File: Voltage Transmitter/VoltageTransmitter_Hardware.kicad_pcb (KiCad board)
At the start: 2 copper layers, 30.5 x 71.9 mm, 8 parts, among them U1 OKI, U2 ESP8266_MCU

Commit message: Gerbs Made
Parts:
- added G***: LOGO, Voltage_Transmitter_Hardware:Austin_Christman_22mmX8.3mm, B.Cu at (127.3, 80.8)
- added G***: LOGO, Voltage_Transmitter_Hardware:John_Beuke_22mmX7.4mm, F.Cu at (138.7, 73.2)
- moved Conn2 2.18 mm to (137.4, 61.7)
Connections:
- C1 pad 2: Net-(C1-Pad2) -> GND
- C2 pad 2: Net-(C1-Pad2) -> GND
- Conn2 pad 1: Net-(C1-Pad2) -> GND
- U1 pad 2: Net-(C1-Pad2) -> GND
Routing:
- net Net-(C1-Pad2): track 26.7 -> 0.00 mm
- net GND: track 5.18 -> 10.3 mm
- net Net-(C1-Pad1): track 18.1 -> 17.1 mm
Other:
- board text added: "Voltage Transmitter, Rev 1 Mars Rover Design Team Missouri S&T, 2019 Austin Christman, John Beuke"
- board text removed: "Voltage Transmitter, Rev 1 Mars Rover Design Team Missouri S&T Austin Christman, John Beuke"

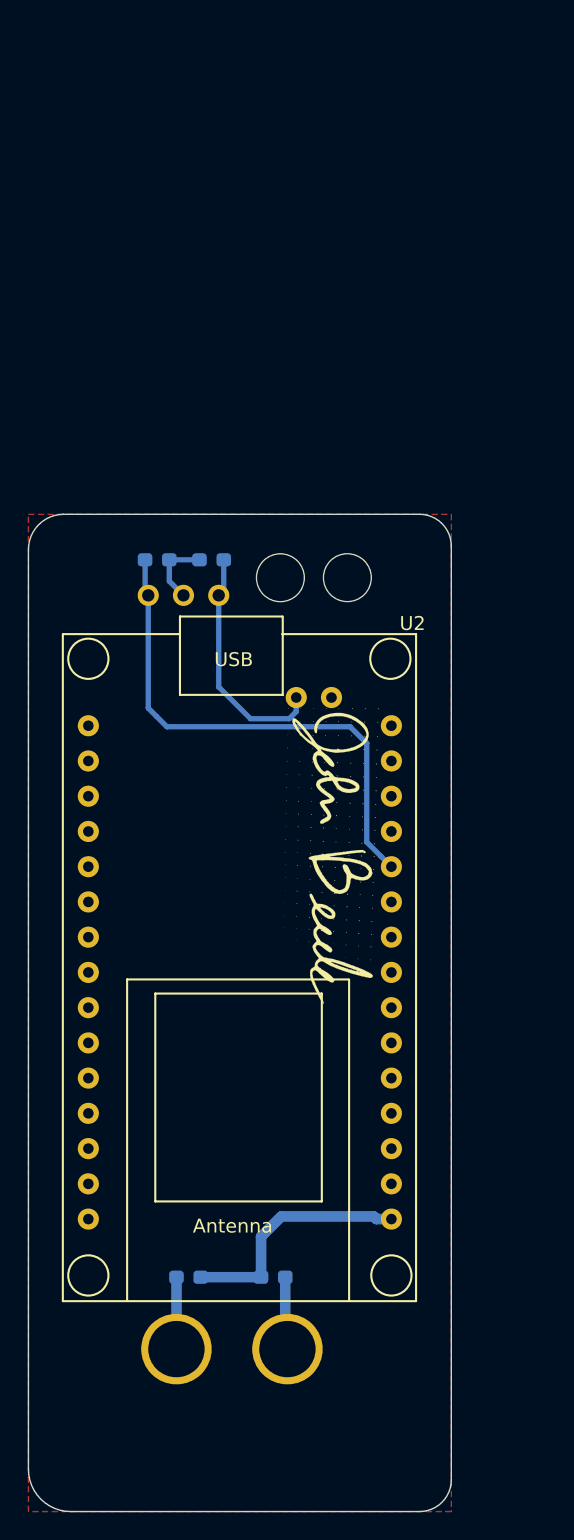
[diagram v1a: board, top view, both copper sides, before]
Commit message: Changed shaped & added comps
Changed to stacked andersons, added power led, transmitting led, and made sure no comps are located on the bottom of the board.
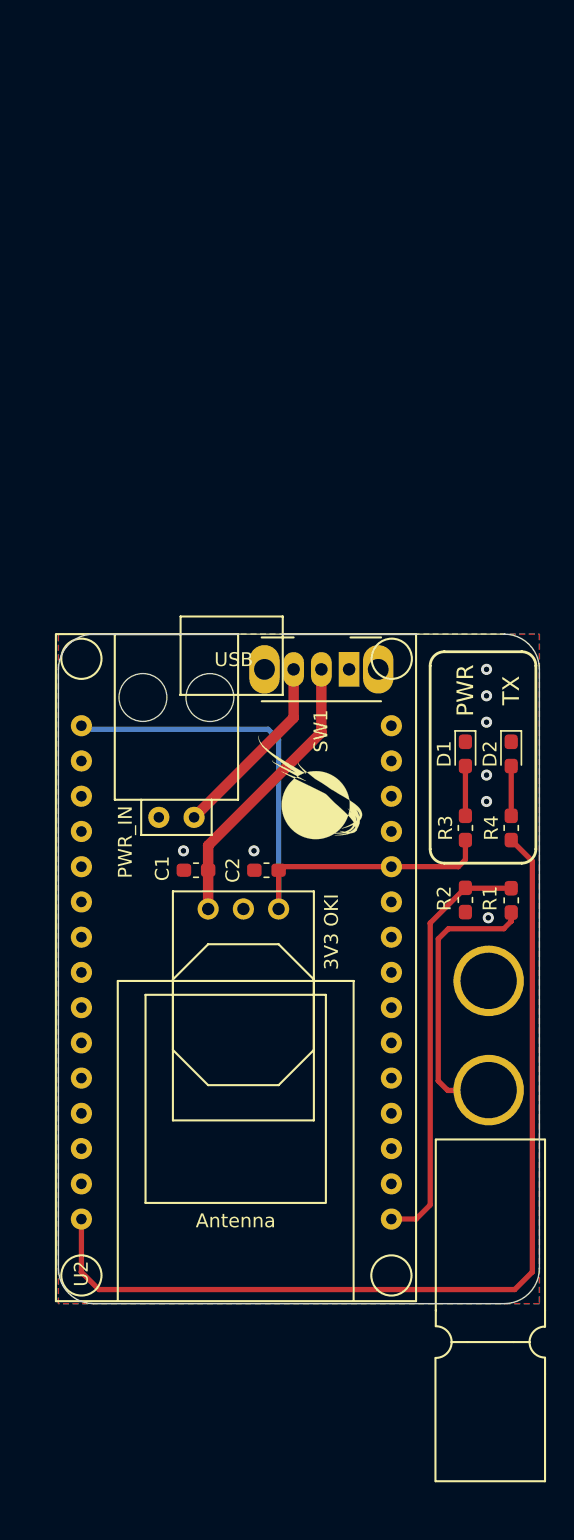
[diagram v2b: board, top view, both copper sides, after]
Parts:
- removed the G*** at (127.3, 80.8)
- added D1: LED, LED_SMD:LED_0603_1608Metric_Pad1.05x0.95mm_HandSolder, F.Cu at (148.3, 65.8)
- added D2: LED, LED_SMD:LED_0603_1608Metric_Pad1.05x0.95mm_HandSolder, F.Cu at (151.6, 65.8)
- added G***: LOGO, MRDT_Silkscreens:z_sig_Jacob_Lipina_Sig_15mm, B.Cu at (128.4, 97.5)
- added G***: LOGO, MRDT_Silkscreens:2_Dahlbot_2.0, B.Cu at (135.8, 68.2)
- added G***: LOGO, MRDT_Silkscreens:0_MRDT_Logo_7.5mm, F.Cu at (137.2, 68.2)
- added R3: 500, Resistor_SMD:R_0603_1608Metric_Pad1.05x0.95mm_HandSolder, F.Cu at (148.3, 71.1)
- added R4: 500, Resistor_SMD:R_0603_1608Metric_Pad1.05x0.95mm_HandSolder, F.Cu at (151.6, 71.1)
- added SW1: SW_Push_SPDT, Button_Switch_THT:SW_CuK_OS102011MA1QN1_SPDT_Angled, F.Cu at (140.0, 59.7)
- C1, C2, Conn2, U1: moved to F.Cu
- Conn1: footprint MRDT_Connectors:Anderson_2_Horisontal_Side_by_Side -> MRDT_Connectors:Anderson_2_Horizontal_Stacked; moved to F.Cu
- G***: moved to B.Cu
- R1: value 100K -> 150K; moved to F.Cu
- R2: value 11K -> 15K; moved to F.Cu
- U2: footprint VoltageTransmitter_Hardware:ESP_8266 NODEMCU -> MRDT_Shields:ESP_8266_NODEMCU
- moved Conn1 34.7 mm to (150.0, 90.0)
- moved R2 33.7 mm to (148.3, 76.3), turned to 270 degrees
- moved R1 32.1 mm to (151.6, 76.3), turned to 90 degrees
- moved C2 23.7 mm to (134.0, 74.2), turned to 180 degrees
- moved U1 23.3 mm to (127.3, 75.7), turned to 0 degrees
- moved C1 22.4 mm to (128.9, 74.2)
- moved G*** 15.7 mm to (125.0, 80.8), turned to 90 degrees
- moved Conn2 13.1 mm to (127.5, 70.4), turned to 0 degrees
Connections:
- Conn1 pad 1: GND -> Net-(Conn1-Pad1)
- Conn1 pad 2: Net-(Conn1-Pad2) -> GND
- Conn2 pad 2: Net-(C1-Pad1) -> Net-(Conn2-Pad2)
- R1 pad 1: Net-(Conn1-Pad2) -> Net-(Conn1-Pad1)
- U2 pad 16: Net-(U2-Pad16) -> +3V3
- U2 pad 30: Net-(U2-Pad30) -> TX_IND
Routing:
- net TX_IND: track 0.00 -> 69.1 mm
- net Net-(Conn1-Pad1): track 0.00 -> 20.6 mm
- net Net-(Conn2-Pad2): track 0.00 -> 13.6 mm
- net Din: track 17.4 -> 30.4 mm
- net GND: track 10.3 -> 2.30 mm, vias 0 -> 8
- net +3V3: track 37.2 -> 44.8 mm
- net Net-(Conn1-Pad2): track 5.25 -> 0.00 mm
- net Net-(D2-Pad2): track 0.00 -> 3.58 mm
- net Net-(D1-Pad2): track 0.00 -> 3.58 mm
- net Net-(C1-Pad1): track 17.1 -> 20.7 mm
- added copper zone on B.Cu, net GND
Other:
- board size 30.5 x 71.9 mm -> 34.7 x 48.3 mm
- board text added: "+"
- board text added: "-"
- board text added: "3V3 OKI"
- board text added: "OFF"
- board text added: "ON"
- board text added: "PWR"
- board text added: "PWR_IN"
- board text added: "TX"
- board text added: "Voltage Transmitter, R2 Mars Rover, Valkyrie Missouri S&T, 2019 Jacob Lipina, John Beuke"
- board text removed: "Voltage Transmitter, Rev 1 Mars Rover Design Team Missouri S&T, 2019 Austin Christman, John Beuke"
